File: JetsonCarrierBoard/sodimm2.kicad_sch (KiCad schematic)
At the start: 1 part

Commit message: Files Autosaved, etc.
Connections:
- no-connect marks 0 -> 6
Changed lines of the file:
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@@
 (kicad_sch (version 20211123) (generator eeschema)
   (paper "A4")
+  (no_connect (at 116.84 99.06))
+  (no_connect (at 116.84 101.6))
+  (no_connect (at 116.84 104.14))
+  (no_connect (at 116.84 106.68))
+  (no_connect (at 116.84 109.22))
+  (no_connect (at 116.84 111.76))
   (symbol (lib_id "SODIMM_Connector:CON_SODIMM260_JETSON_NANO") (at 143.51 95.25 0) (unit 2)
     (in_bom yes) (on_board yes) (fields_autoplaced)

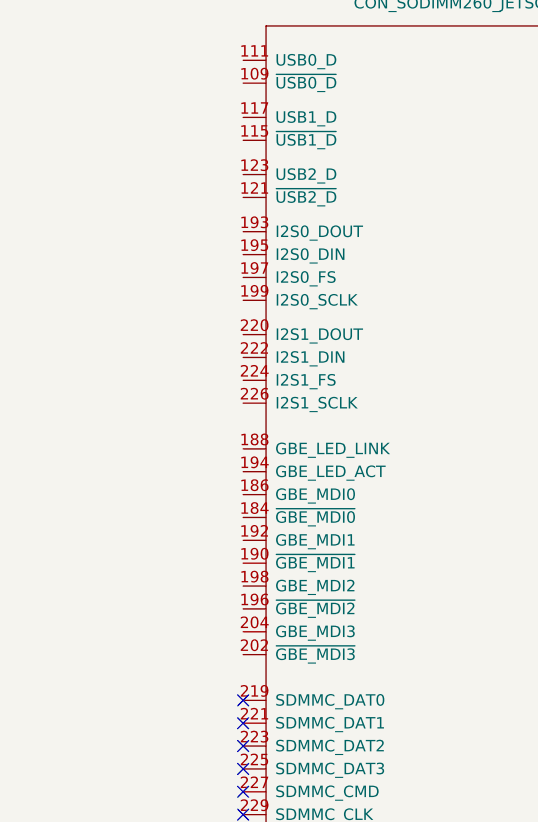
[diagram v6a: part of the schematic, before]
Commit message: Continued M.2 WiFi connections
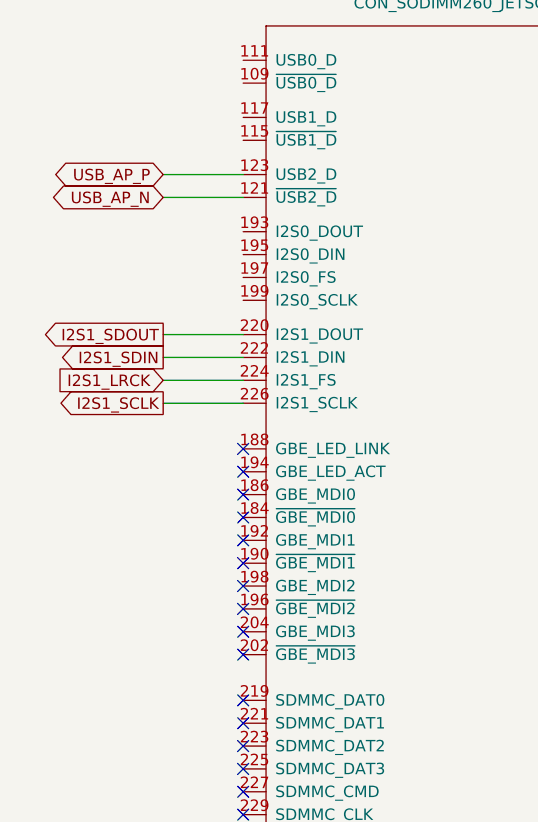
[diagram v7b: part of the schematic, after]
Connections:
- net USB_AP_N: now reaches J?.121 (~{USB2_D})
- net USB_AP_P: now reaches J?.123 (USB2_D)
- net I2S1_SDOUT: now reaches J?.220 (I2S1_DOUT)
- net I2S1_SDIN: now reaches J?.222 (I2S1_DIN)
- net I2S1_LRCK: now reaches J?.224 (I2S1_FS)
- net I2S1_SCLK: now reaches J?.226 (I2S1_SCLK)
- no-connect marks 6 -> 16
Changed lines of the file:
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@@
   (no_connect (at 116.84 109.22))
   (no_connect (at 116.84 111.76))
+  (no_connect (at 116.84 83.82))
+  (no_connect (at 116.84 86.36))
+  (no_connect (at 116.84 88.9))
+  (no_connect (at 116.84 91.44))
+  (no_connect (at 116.84 93.98))
+  (no_connect (at 116.84 71.12))
+  (no_connect (at 116.84 73.66))
+  (no_connect (at 116.84 76.2))
+  (no_connect (at 116.84 78.74))
+  (no_connect (at 116.84 81.28))
+  (wire (pts (xy 107.95 63.5) (xy 116.84 63.5))
+    (stroke (width 0) (type default) (color 0 0 0 0))
+  )
+  (wire (pts (xy 107.95 43.18) (xy 116.84 43.18))
+    (stroke (width 0) (type default) (color 0 0 0 0))
+  )
+  (wire (pts (xy 107.95 66.04) (xy 116.84 66.04))
+    (stroke (width 0) (type default) (color 0 0 0 0))
+  )
+  (wire (pts (xy 107.95 58.42) (xy 116.84 58.42))
+    (stroke (width 0) (type default) (color 0 0 0 0))
+  )
+  (wire (pts (xy 107.95 60.96) (xy 116.84 60.96))
+    (stroke (width 0) (type default) (color 0 0 0 0))
+  )
+  (wire (pts (xy 107.95 40.64) (xy 116.84 40.64))
+    (stroke (width 0) (type default) (color 0 0 0 0))
+  )
+  (global_label "I2S1_SDOUT" (shape output) (at 107.95 58.42 180) (fields_autoplaced)
+    (effects (font (size 1.27 1.27)) (justify right))
+    (property "Intersheet References" "${INTERSHEET_REFS}" (id 0) (at 94.2279 58.3406 0)
+      (effects (font (size 1.27 1.27)) (justify right) hide)
+    )
+  )
+  (global_label "USB_AP_P" (shape bidirectional) (at 107.95 40.64 180) (fields_autoplaced)
+    (effects (font (size 1.27 1.27)) (justify right))
+    (property "Intersheet References" "${INTERSHEET_REFS}" (id 0) (at 96.1631 40.7194 0)
+      (effects (font (size 1.27 1.27)) (justify right) hide)
+    )
+  )
+  (global_label "I2S1_SCLK" (shape output) (at 107.95 66.04 180) (fields_autoplaced)
+    (effects (font (size 1.27 1.27)) (justify right))
+    (property "Intersheet References" "${INTERSHEET_REFS}" (id 0) (at 95.5583 65.9606 0)
+      (effects (font (size 1.27 1.27)) (justify right) hide)
+    )
+  )
+  (global_label "I2S1_SDIN" (shape output) (at 107.95 60.96 180) (fields_autoplaced)
+    (effects (font (size 1.27 1.27)) (justify right))
+    (property "Intersheet References" "${INTERSHEET_REFS}" (id 0) (at 95.9212 60.8806 0)
+      (effects (font (size 1.27 1.27)) (justify right) hide)
+    )
+  )
+  (global_label "I2S1_LRCK" (shape input) (at 107.95 63.5 180) (fields_autoplaced)
+    (effects (font (size 1.27 1.27)) (justify right))
+    (property "Intersheet References" "${INTERSHEET_REFS}" (id 0) (at 95.4979 63.4206 0)
+      (effects (font (size 1.27 1.27)) (justify right) hide)
+    )
+  )
+  (global_label "USB_AP_N" (shape bidirectional) (at 107.95 43.18 180) (fields_autoplaced)
+    (effects (font (size 1.27 1.27)) (justify right))
+    (property "Intersheet References" "${INTERSHEET_REFS}" (id 0) (at 96.1026 43.2594 0)
+      (effects (font (size 1.27 1.27)) (justify right) hide)
+    )
+  )
   (symbol (lib_id "SODIMM_Connector:CON_SODIMM260_JETSON_NANO") (at 143.51 95.25 0) (unit 2)
     (in_bom yes) (on_board yes) (fields_autoplaced)
